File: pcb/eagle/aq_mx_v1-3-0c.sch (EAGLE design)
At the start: 36 parts, among them J1 DB9-MALE-RA, J2 DB9-MALE-RA, Q1 BC548, U1 CY62256LL-PC, U2 AY-3-8910, U3 27C512AP, U4 GAL16V8, U5 74LS74N, U6 GAL16V8, U7 74LS244N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

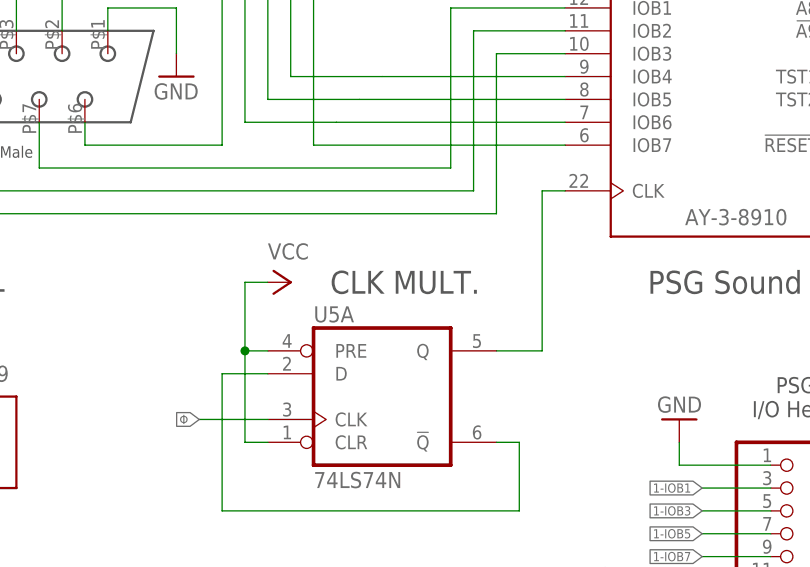
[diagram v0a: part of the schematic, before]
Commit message: Schematic updates
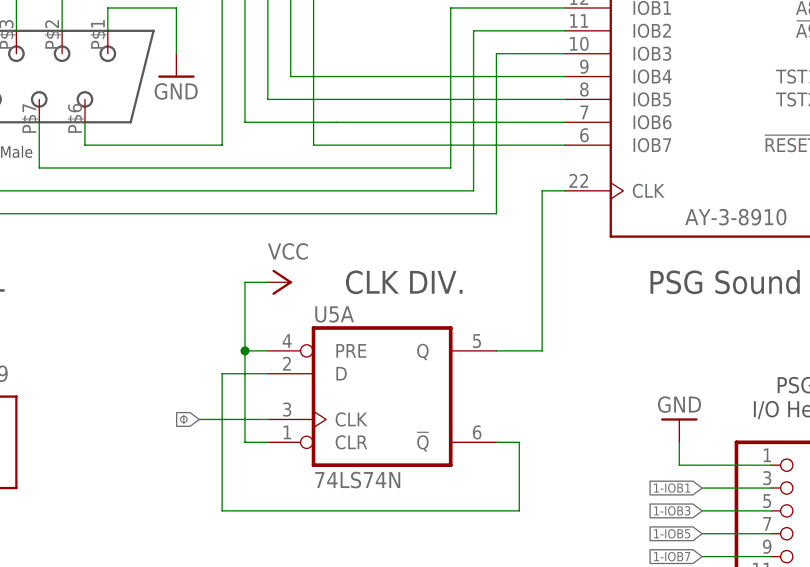
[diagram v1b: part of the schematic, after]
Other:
- note added: "CLK DIV."
- note removed: "CLK MULT."
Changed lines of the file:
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@@
 <text x="-71.12" y="-20.32" size="2.54" layer="97" align="center">RAM</text>
 <text x="-124.46" y="-17.78" size="2.54" layer="97" align="center">ROM</text>
-<text x="35.56" y="0" size="2.54" layer="97" align="center">CLK MULT.</text>
+<text x="35.56" y="0" size="2.54" layer="97" align="center">CLK DIV.</text>
 <text x="-13.97" y="-2.032" size="2.54" layer="97" align="center">RESET</text>
 <text x="186.69" y="-17.526" size="1.778" layer="97" align="bottom-center">CH376S USB
